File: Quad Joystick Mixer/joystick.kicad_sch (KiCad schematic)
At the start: 14 parts, among them U4 OPA1692xD

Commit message: progress on schematic
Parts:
- removed R62, R63: 5.1k, symbol Device:R_US
- removed RV3: Joystick - 10k, symbol Device:R_Potentiometer_Dual_Separate
- added RV3, RV4: 10k-B, Eyewool Pots:StomboxParts_9MM, symbol Device:R_Potentiometer_US
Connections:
- net Earth: now also RV3.1, RV4.1
- net +3.3V: now reaches C13.1
- net +3.3V: now also C13.1, RV3.3, RV4.3
- net at R64.1: now also RV3.2
- net at R65.1: now also RV4.2

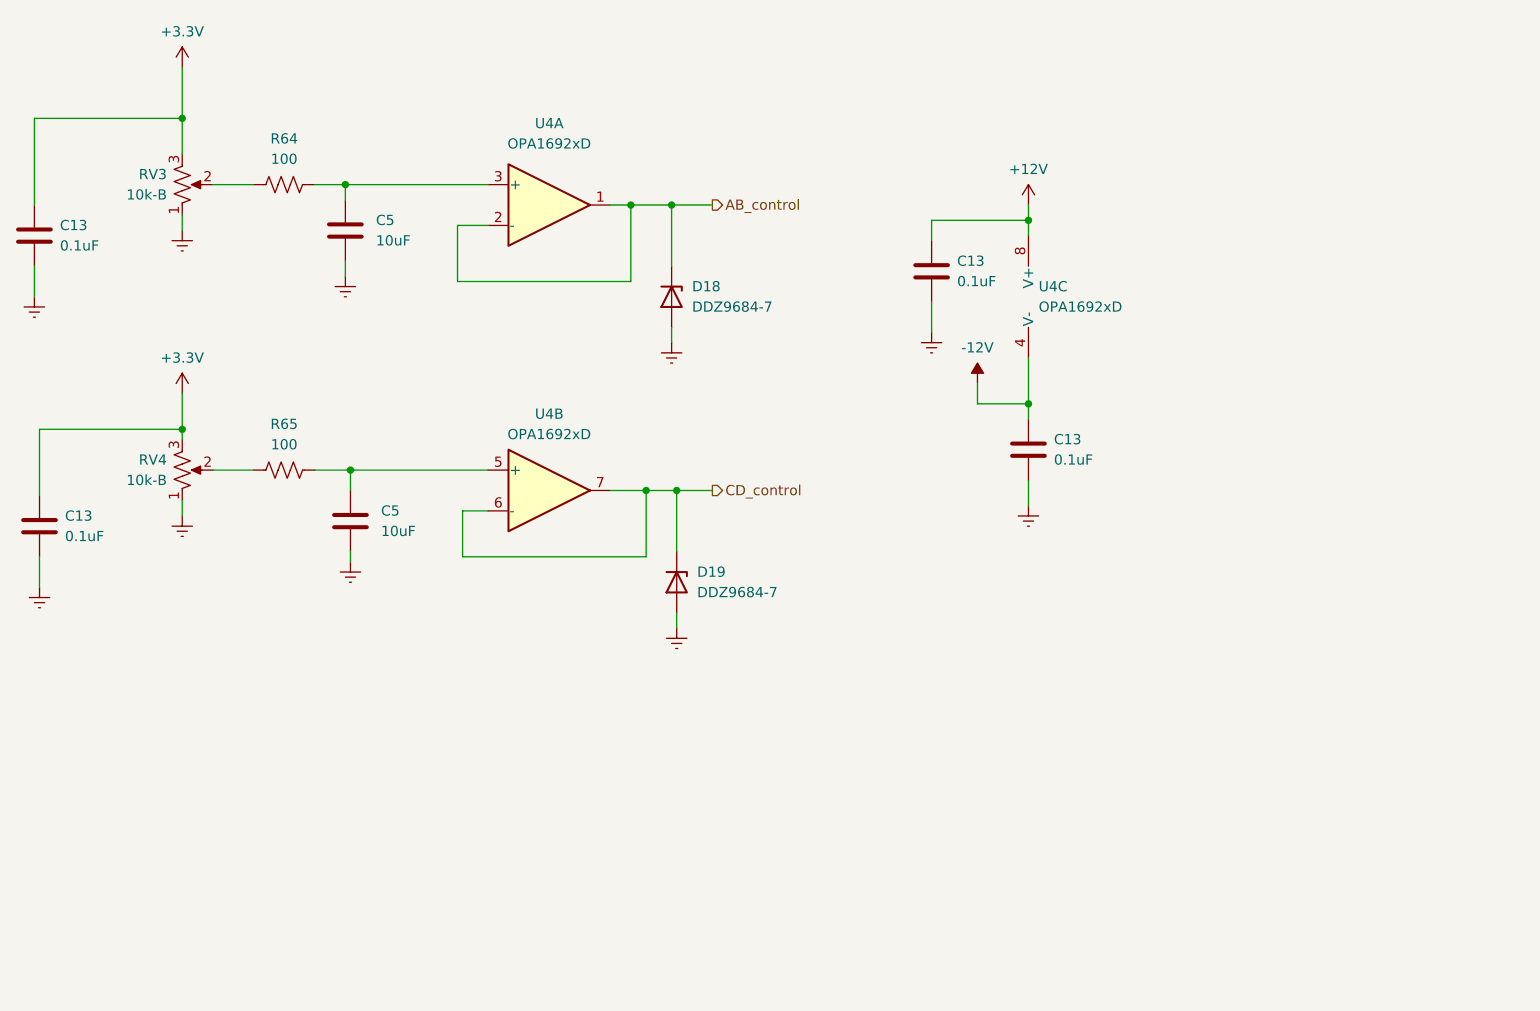
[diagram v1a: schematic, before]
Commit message: add in rotary circuit and some docs
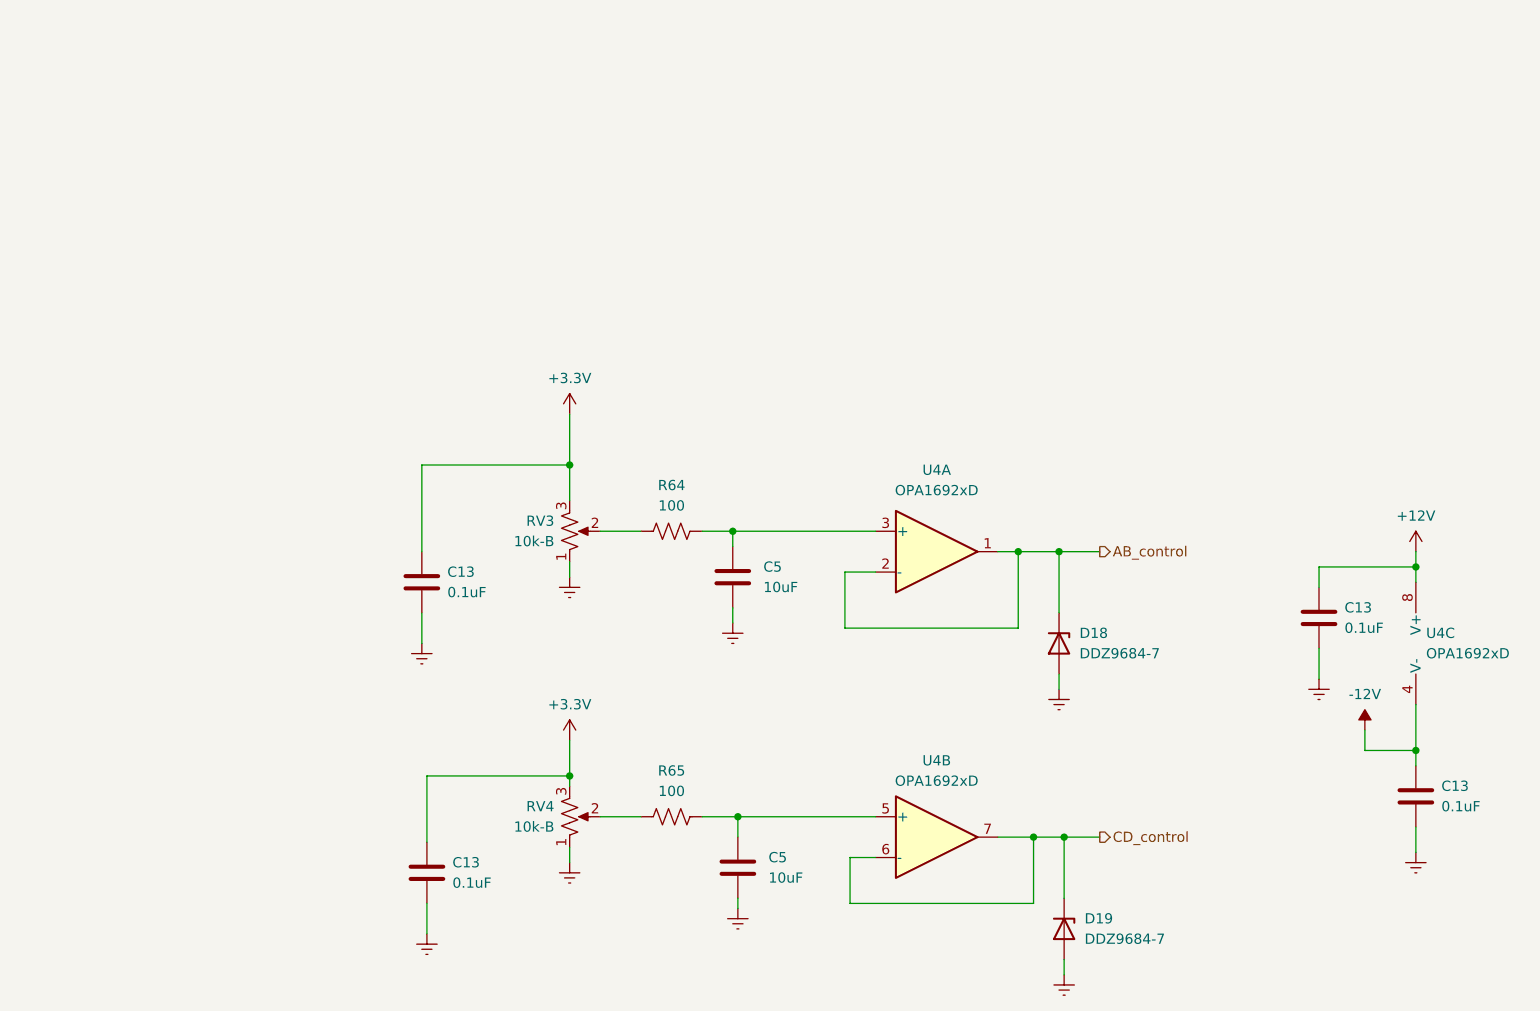
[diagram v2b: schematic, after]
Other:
- moved on the sheet: C13, C5, D18, D19, R64, R65, RV3, RV4, U4A, U4B, U4C
